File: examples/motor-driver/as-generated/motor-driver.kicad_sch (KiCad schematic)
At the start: 15 parts, among them J1 VM 2.7-10.8V, J2 MOTOR A, J3 MOTOR B, J4 LOGIC, U1 DRV8833PW

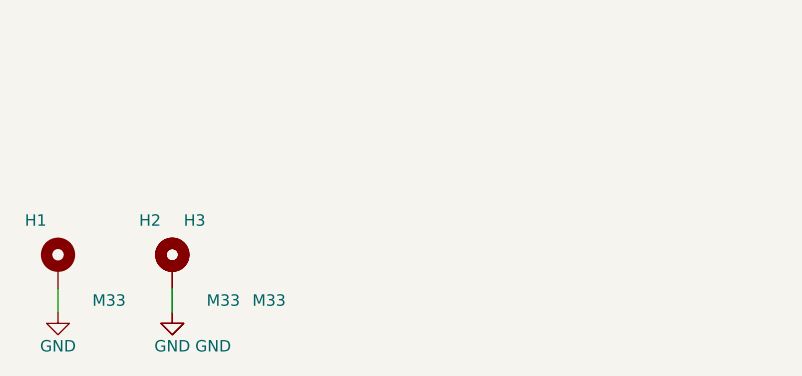
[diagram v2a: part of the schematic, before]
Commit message: Give the assembly machine something to aim at
Fiducials: three copper dots in bare mask windows, near three different
corners so a pick-and-place gets rotation as well as offset. It aligns
to the board, not to the drawing - without them it has only the routed
outline, cut to a tolerance ten times looser than the placement a 0.5 mm
pitch part is asking for. `fab.no_fiducials` reports a fine-pitch board
that has none, as context rather than as a fault: plenty of boards are
built one at a time with tweezers.

They share the corner search with the mounting holes, which is where
this found a real bug: `_courtyard_box` read lines and rectangles only,
and a mounting hole draws its courtyard as one circle - so every hole
measured as taking up no room at all, and the first three fiducials
landed on top of three screw holes. Circles and arcs count now.

Co-Authored-By: Claude Fable 5 <noreply@anthropic.com>
Claude-Session: https://claude.ai/code/session_01DUj7Ltu92tWg159mCSacwY
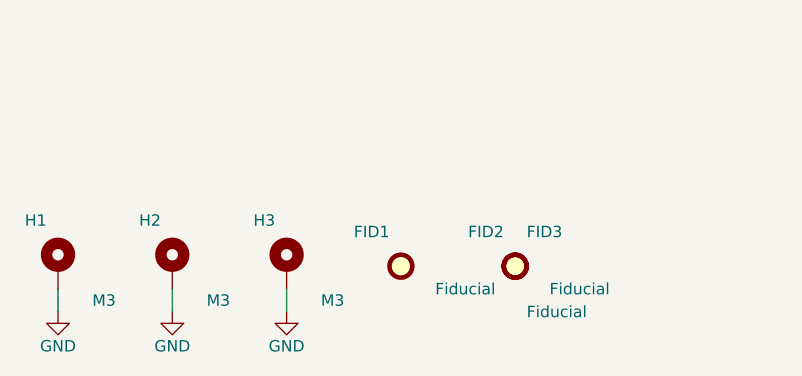
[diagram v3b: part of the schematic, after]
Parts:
- added FID1, FID2, FID3: Fiducial, Fiducial:Fiducial_1mm_Mask2mm, symbol Mechanical:Fiducial
- H1, H2, H3: value M33 -> M3
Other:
- moved on the sheet: H3
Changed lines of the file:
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@@
     (exclude_from_sim no) (in_bom yes) (on_board yes) (dnp no)
     (property "Reference" "H1" (at 24.44 164.91 0) (effects (font (size 1.27 1.27)) (justify right)))
-    (property "Value" "M33" (at 29.52 173.8 0) (effects (font (size 1.27 1.27)) (justify left)))
+    (property "Value" "M3" (at 29.52 173.8 0) (effects (font (size 1.27 1.27)) (justify left)))
     (property "Footprint" "MountingHole:MountingHole_3.2mm_M3_Pad" (at 25.71 169.99 0) (effects (font (size 1.27 1.27)) hide))
     (property "Datasheet" "~" (at 25.71 169.99 0) (effects (font (size 1.27 1.27)) hide))
@@
     (exclude_from_sim no) (in_bom yes) (on_board yes) (dnp no)
     (property "Reference" "H2" (at 37.14 164.91 0) (effects (font (size 1.27 1.27)) (justify right)))
-    (property "Value" "M33" (at 42.22 173.8 0) (effects (font (size 1.27 1.27)) (justify left)))
+    (property "Value" "M3" (at 42.22 173.8 0) (effects (font (size 1.27 1.27)) (justify left)))
     (property "Footprint" "MountingHole:MountingHole_3.2mm_M3_Pad" (at 38.41 169.99 0) (effects (font (size 1.27 1.27)) hide))
     (property "Datasheet" "~" (at 38.41 169.99 0) (effects (font (size 1.27 1.27)) hide))
@@
     (instances (project "motor-driver" (path "/bddeec65-fa67-5f6a-9af2-d98e98d56e38" (reference "H2") (unit 1))))
   )
-  (wire (pts (xy 38.41 172.53) (xy 38.41 175.07)) (stroke (width 0) (type default)))
-  (symbol (lib_id "Mechanical:MountingHole_Pad") (at 38.41 169.99 0.0) (unit 1)
+  (wire (pts (xy 51.11 172.53) (xy 51.11 175.07)) (stroke (width 0) (type default)))
+  (symbol (lib_id "Mechanical:MountingHole_Pad") (at 51.11 169.99 0.0) (unit 1)
     (exclude_from_sim no) (in_bom yes) (on_board yes) (dnp no)
-    (property "Reference" "H3" (at 39.68 164.91 0) (effects (font (size 1.27 1.27)) (justify left)))
-    (property "Value" "M33" (at 47.3 173.8 0) (effects (font (size 1.27 1.27)) (justify left)))
-    (property "Footprint" "MountingHole:MountingHole_3.2mm_M3_Pad" (at 38.41 169.99 0) (effects (font (size 1.27 1.27)) hide))
-    (property "Datasheet" "~" (at 38.41 169.99 0) (effects (font (size 1.27 1.27)) hide))
+    (property "Reference" "H3" (at 49.84 164.91 0) (effects (font (size 1.27 1.27)) (justify right)))
+    (property "Value" "M3" (at 54.92 173.8 0) (effects (font (size 1.27 1.27)) (justify left)))
+    (property "Footprint" "MountingHole:MountingHole_3.2mm_M3_Pad" (at 51.11 169.99 0) (effects (font (size 1.27 1.27)) hide))
+    (property "Datasheet" "~" (at 51.11 169.99 0) (effects (font (size 1.27 1.27)) hide))
     (pin "1" (uuid "b09ff8b6-9110-54ce-9289-a4d5206e7444-p1"))
     (instances (project "motor-driver" (path "/bddeec65-fa67-5f6a-9af2-d98e98d56e38" (reference "H3") (unit 1))))
+  )
+  (symbol (lib_id "Mechanical:Fiducial") (at 63.81 169.99 0.0) (unit 1)
+    (exclude_from_sim no) (in_bom yes) (on_board yes) (dnp no)
+    (property "Reference" "FID1" (at 62.54 166.18 0) (effects (font (size 1.27 1.27)) (justify right)))
+    (property "Value" "Fiducial" (at 67.62 172.53 0) (effects (font (size 1.27 1.27)) (justify left)))
+    (property "Footprint" "Fiducial:Fiducial_1mm_Mask2mm" (at 63.81 169.99 0) (effects (font (size 1.27 1.27)) hide))
+    (property "Datasheet" "~" (at 63.81 169.99 0) (effects (font (size 1.27 1.27)) hide))
+    (instances (project "motor-driver" (path "/bddeec65-fa67-5f6a-9af2-d98e98d56e38" (reference "FID1") (unit 1))))
+  )
+  (symbol (lib_id "Mechanical:Fiducial") (at 76.51 169.99 0.0) (unit 1)
+    (exclude_from_sim no) (in_bom yes) (on_board yes) (dnp no)
+    (property "Reference" "FID2" (at 75.24 166.18 0) (effects (font (size 1.27 1.27)) (justify right)))
+    (property "Value" "Fiducial" (at 80.32 172.53 0) (effects (font (size 1.27 1.27)) (justify left)))
+    (property "Footprint" "Fiducial:Fiducial_1mm_Mask2mm" (at 76.51 169.99 0) (effects (font (size 1.27 1.27)) hide))
+    (property "Datasheet" "~" (at 76.51 169.99 0) (effects (font (size 1.27 1.27)) hide))
+    (instances (project "motor-driver" (path "/bddeec65-fa67-5f6a-9af2-d98e98d56e38" (reference "FID2") (unit 1))))
+  )
+  (symbol (lib_id "Mechanical:Fiducial") (at 76.51 169.99 0.0) (unit 1)
+    (exclude_from_sim no) (in_bom yes) (on_board yes) (dnp no)
+    (property "Reference" "FID3" (at 77.78 166.18 0) (effects (font (size 1.27 1.27)) (justify left)))
+    (property "Value" "Fiducial" (at 77.78 175.07 0) (effects (font (size 1.27 1.27)) (justify left)))
+    (property "Footprint" "Fiducial:Fiducial_1mm_Mask2mm" (at 76.51 169.99 0) (effects (font (size 1.27 1.27)) hide))
+    (property "Datasheet" "~" (at 76.51 169.99 0) (effects (font (size 1.27 1.27)) hide))
+    (instances (project "motor-driver" (path "/bddeec65-fa67-5f6a-9af2-d98e98d56e38" (reference "FID3") (unit 1))))
   )
   (wire (pts (xy 46.03 82.36) (xy 53.65 82.36)) (stroke (width 0) (type default)))
@@
     (instances (project "motor-driver" (path "/bddeec65-fa67-5f6a-9af2-d98e98d56e38" (reference "#PWR10") (unit 1))))
   )
-  (symbol (lib_id "power:GND") (at 38.41 175.07 0) (unit 1)
+  (symbol (lib_id "power:GND") (at 51.11 175.07 0) (unit 1)
     (exclude_from_sim no) (in_bom no) (on_board yes) (dnp no)
-    (property "Reference" "#PWR11" (at 38.41 175.07 0) (effects (font (size 1.27 1.27)) hide))
-    (property "Value" "GND" (at 40.95 178.88 0) (effects (font (size 1.27 1.27)) (justify left)))
-    (property "Footprint" "" (at 38.41 175.07 0) (effects (font (size 1.27 1.27)) hide))
-    (property "Datasheet" "" (at 38.41 175.07 0) (effects (font (size 1.27 1.27)) hide))
+    (property "Reference" "#PWR11" (at 51.11 175.07 0) (effects (font (size 1.27 1.27)) hide))
+    (property "Value" "GND" (at 51.11 178.88 0) (effects (font (size 1.27 1.27))))
+    (property "Footprint" "" (at 51.11 175.07 0) (effects (font (size 1.27 1.27)) hide))
+    (property "Datasheet" "" (at 51.11 175.07 0) (effects (font (size 1.27 1.27)) hide))
     (pin "1" (uuid "36f47f82-b430-5f2e-8c28-879d8277211b-p"))
     (instances (project "motor-driver" (path "/bddeec65-fa67-5f6a-9af2-d98e98d56e38" (reference "#PWR11") (unit 1))))

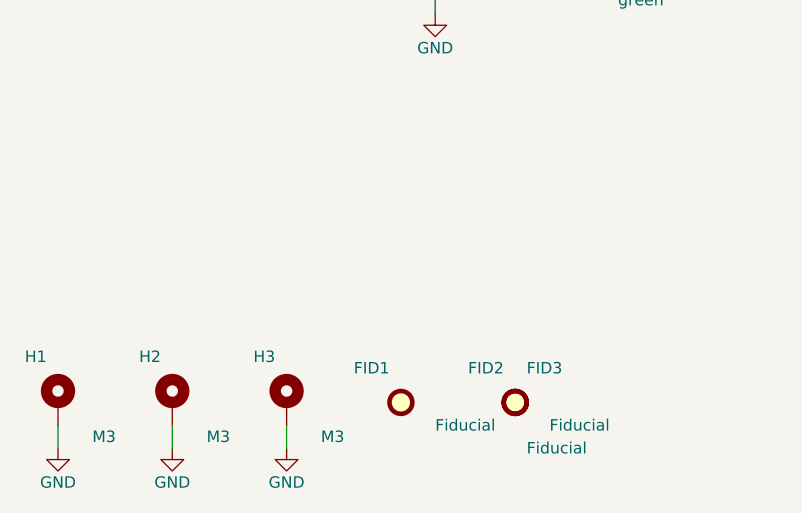
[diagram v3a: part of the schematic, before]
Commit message: Let the new parts sit somewhere sensible, on the board and on the sheet
Placing screw holes and fiducials turned up four things that were wrong
before either existed, all of them about where something is allowed to
go rather than about the parts themselves.

A designator was kept off the pads but not inside the board outline, so
any part at the edge - a connector, and now a hole - had its reference
clipped by the edge. Every board had been carrying one or two of those.

A symbol with no pins leaves no trace in the sheet planner's obstacle
list, because that list is built from pin stubs. The screw holes were
invisible to it and the fiducials landed on top of them. The free-row
search also ran off the right-hand edge of an A4 page and sat over the
title block on the way, which is `readability.outside_page` and
`readability.margin_intrusion` respectively - both real, both now
avoided by bounding the search to the drawing area.

And the bill-of-materials flag is read from the footprint rather than
the symbol library, because the footprint is the side KiCad's parity
check reads and the side the fab agrees with. That retired three
warnings the op-amp board had been carrying since it gained test
points: `Connector:TestPoint` claims to be a BOM line and its own
footprint says otherwise.

All four fast boards pass their gates; the suite is green on 10.0.4.

Co-Authored-By: Claude Fable 5 <noreply@anthropic.com>
Claude-Session: https://claude.ai/code/session_01DUj7Ltu92tWg159mCSacwY
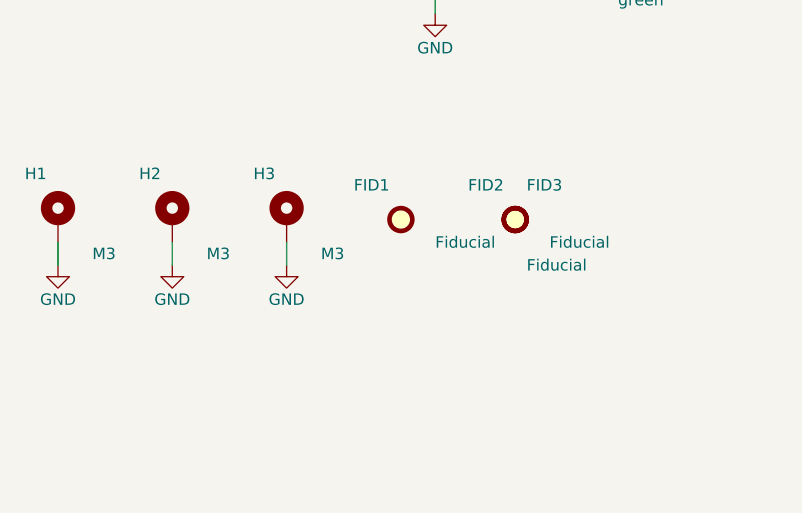
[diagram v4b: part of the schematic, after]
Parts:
- FID1, FID2, FID3, H1, H2, H3: now left out of the parts list
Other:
- moved on the sheet: FID1, FID2, FID3, H1, H2, H3

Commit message: Put the vias back where the copper moved, and let the fillets vote
The FPGA board came back from its re-route with two unconnected nets and
three dangling ends, and the cause was older than anything this round
added. The router hands back a via for every layer change; six passes
then reshape the copper - snapping to 45s, chamfering, spreading folds,
and now filleting - and none of them move the holes underneath. A joint
that slides a millimetre from its via is two loose ends and one broken
net, and `_unlooped` then swept the via away as orphaned, because it
kept a via only when a track ended on its exact coordinate.

Two fixes, both about what "connected" means. A via lives if kept copper
*touches* it, not if a coordinate matches. And a new `_joined` pass
re-derives the joints from the copper that actually got written: where a
net ends on two layers at one point with no via reaching it, one goes
back in. It reads the finished geometry, so it cannot drift the way six
separate passes carrying vias along with them would.

The same reasoning fixes two rules that had been measuring coordinates
rather than copper. `route.stub` matched a track end to a via's centre
exactly, and called a joint a stub whenever a reshaping pass had moved
it a quarter of a millimetre inside the very barrel it was connected to.
`route.width_step` walked a neck back to its pad and stopped at the
first width change - which, on a filleted board, is the teardrop, so
every escape's neck stopped being recognised as one.

While the three copies of the post-route pipeline were being edited for
the third time this session, they became one function. That is how
`_teardrops` had come to run on two of the three exits.

All five boards: DRC clean on both matrix versions, nothing unconnected.
Four pass their gates; the FPGA board is down to the two-layer bill it
has always had - four nets over plane cuts and one 88 degree corner.

Co-Authored-By: Claude Fable 5 <noreply@anthropic.com>
Claude-Session: https:/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
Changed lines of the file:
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@@
     (exclude_from_sim no) (in_bom no) (on_board yes) (dnp no)
     (property "Reference" "H1" (at 24.44 144.59 0) (effects (font (size 1.27 1.27)) (justify right)))
-    (property "Value" "M3" (at 29.52 153.48 0) (effects (font (size 1.27 1.27)) (justify left)))
+    (property "Value" "M3" (at 29.52 153.48 0) (effects (font (size 1.27 1.27)) (justify left) hide))
     (property "Footprint" "MountingHole:MountingHole_3.2mm_M3_Pad" (at 25.71 149.67 0) (effects (font (size 1.27 1.27)) hide))
     (property "Datasheet" "~" (at 25.71 149.67 0) (effects (font (size 1.27 1.27)) hide))
@@
     (exclude_from_sim no) (in_bom no) (on_board yes) (dnp no)
     (property "Reference" "H2" (at 37.14 144.59 0) (effects (font (size 1.27 1.27)) (justify right)))
-    (property "Value" "M3" (at 42.22 153.48 0) (effects (font (size 1.27 1.27)) (justify left)))
+    (property "Value" "M3" (at 42.22 153.48 0) (effects (font (size 1.27 1.27)) (justify left) hide))
     (property "Footprint" "MountingHole:MountingHole_3.2mm_M3_Pad" (at 38.41 149.67 0) (effects (font (size 1.27 1.27)) hide))
     (property "Datasheet" "~" (at 38.41 149.67 0) (effects (font (size 1.27 1.27)) hide))
@@
     (exclude_from_sim no) (in_bom no) (on_board yes) (dnp no)
     (property "Reference" "H3" (at 49.84 144.59 0) (effects (font (size 1.27 1.27)) (justify right)))
-    (property "Value" "M3" (at 54.92 153.48 0) (effects (font (size 1.27 1.27)) (justify left)))
+    (property "Value" "M3" (at 54.92 153.48 0) (effects (font (size 1.27 1.27)) (justify left) hide))
     (property "Footprint" "MountingHole:MountingHole_3.2mm_M3_Pad" (at 51.11 149.67 0) (effects (font (size 1.27 1.27)) hide))
     (property "Datasheet" "~" (at 51.11 149.67 0) (effects (font (size 1.27 1.27)) hide))
@@
     (exclude_from_sim no) (in_bom no) (on_board yes) (dnp no)
     (property "Reference" "FID1" (at 62.54 145.86 0) (effects (font (size 1.27 1.27)) (justify right)))
-    (property "Value" "Fiducial" (at 67.62 152.21 0) (effects (font (size 1.27 1.27)) (justify left)))
+    (property "Value" "Fiducial" (at 67.62 152.21 0) (effects (font (size 1.27 1.27)) (justify left) hide))
     (property "Footprint" "Fiducial:Fiducial_1mm_Mask2mm" (at 63.81 149.67 0) (effects (font (size 1.27 1.27)) hide))
     (property "Datasheet" "~" (at 63.81 149.67 0) (effects (font (size 1.27 1.27)) hide))
@@
     (exclude_from_sim no) (in_bom no) (on_board yes) (dnp no)
     (property "Reference" "FID2" (at 75.24 145.86 0) (effects (font (size 1.27 1.27)) (justify right)))
-    (property "Value" "Fiducial" (at 80.32 152.21 0) (effects (font (size 1.27 1.27)) (justify left)))
+    (property "Value" "Fiducial" (at 80.32 152.21 0) (effects (font (size 1.27 1.27)) (justify left) hide))
     (property "Footprint" "Fiducial:Fiducial_1mm_Mask2mm" (at 76.51 149.67 0) (effects (font (size 1.27 1.27)) hide))
     (property "Datasheet" "~" (at 76.51 149.67 0) (effects (font (size 1.27 1.27)) hide))
@@
     (exclude_from_sim no) (in_bom no) (on_board yes) (dnp no)
     (property "Reference" "FID3" (at 77.78 145.86 0) (effects (font (size 1.27 1.27)) (justify left)))
-    (property "Value" "Fiducial" (at 77.78 154.75 0) (effects (font (size 1.27 1.27)) (justify left)))
+    (property "Value" "Fiducial" (at 77.78 154.75 0) (effects (font (size 1.27 1.27)) (justify left) hide))
     (property "Footprint" "Fiducial:Fiducial_1mm_Mask2mm" (at 76.51 149.67 0) (effects (font (size 1.27 1.27)) hide))
     (property "Datasheet" "~" (at 76.51 149.67 0) (effects (font (size 1.27 1.27)) hide))

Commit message: Leave room for the screw, and print the ink where the board is
The screw holes were placed against the hole's own courtyard, which is the
drill plus a whisker - so on four of the five boards a hole sat inside a
connector's mating space, closest 0.42 mm. What goes through an M3 hole is a
pan head on a washer, seven millimetres of steel lying flat, and a connector
wants its shell, its wires and the fingers that fit them on top of that. The
spot search now keeps the fastener's own circle clear of every part body and
gives connectors CONNECTOR_ACCESS more, and three rules say so when a board
does not: mechanical.fastener_clearance, mechanical.connector_access and
mechanical.fastener_copper, all blocking for a generated design.

Silk was measured with a per-character advance of 0.78, and KiCad's stroke
font is proportional at 0.94 to 1.07. Everything downstream of that estimate
was placing ink where it did not fit: a legend across a capacitor's land, a
designator through the board's own name. `_text_extent` takes the top of the
measured range, adds the fab's clearance and is used by every silk placement.

Three placements also fell through to a position nobody chose. A designator
that found nothing kept its library offset, which for a part in a corner
points off the board; the board id took the first of eight fixed strips; a
legend took the least bad of six spots. All three are scored now, over
candidate sets wide enough to have an answer - and a pad-less footprint, which
is what a mounting hole is, is no longer skipped outright.

silk.off_board reports the case KiCad's own test cannot: ink that clears the
edge entirely is never printed, and DRC only measures ink that crosses it.

_unspiked redraws a corner tighter than a right angle as the elbow between its
neighbours - one diagonal, one straight, no step back to a heading the line
has already left. It is never longer than what it replaces.

All four fast boards: 0 errors, 0 warnings.

Co-Authored-By: Claude Fable 5 <no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
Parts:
- removed FID3: Fiducial, Fiducial:Fiducial_1mm_Mask2mm, symbol Mechanical:Fiducial
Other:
- moved on the sheet: FID2
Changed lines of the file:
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@@
     (instances (project "motor-driver" (path "/bddeec65-fa67-5f6a-9af2-d98e98d56e38" (reference "FID1") (unit 1))))
   )
-  (symbol (lib_id "Mechanical:Fiducial") (at 76.51 149.67 0.0) (unit 1)
+  (symbol (lib_id "Mechanical:Fiducial") (at 63.81 149.67 0.0) (unit 1)
     (exclude_from_sim no) (in_bom no) (on_board yes) (dnp no)
-    (property "Reference" "FID2" (at 75.24 145.86 0) (effects (font (size 1.27 1.27)) (justify right)))
-    (property "Value" "Fiducial" (at 80.32 152.21 0) (effects (font (size 1.27 1.27)) (justify left) hide))
-    (property "Footprint" "Fiducial:Fiducial_1mm_Mask2mm" (at 76.51 149.67 0) (effects (font (size 1.27 1.27)) hide))
-    (property "Datasheet" "~" (at 76.51 149.67 0) (effects (font (size 1.27 1.27)) hide))
+    (property "Reference" "FID2" (at 65.08 145.86 0) (effects (font (size 1.27 1.27)) (justify left)))
+    (property "Value" "Fiducial" (at 65.08 154.75 0) (effects (font (size 1.27 1.27)) (justify left) hide))
+    (property "Footprint" "Fiducial:Fiducial_1mm_Mask2mm" (at 63.81 149.67 0) (effects (font (size 1.27 1.27)) hide))
+    (property "Datasheet" "~" (at 63.81 149.67 0) (effects (font (size 1.27 1.27)) hide))
     (instances (project "motor-driver" (path "/bddeec65-fa67-5f6a-9af2-d98e98d56e38" (reference "FID2") (unit 1))))
   )
-  (symbol (lib_id "Mechanical:Fiducial") (at 76.51 149.67 0.0) (unit 1)
-    (exclude_from_sim no) (in_bom no) (on_board yes) (dnp no)
-    (property "Reference" "FID3" (at 77.78 145.86 0) (effects (font (size 1.27 1.27)) (justify left)))
-    (property "Value" "Fiducial" (at 77.78 154.75 0) (effects (font (size 1.27 1.27)) (justify left) hide))
-    (property "Footprint" "Fiducial:Fiducial_1mm_Mask2mm" (at 76.51 149.67 0) (effects (font (size 1.27 1.27)) hide))
-    (property "Datasheet" "~" (at 76.51 149.67 0) (effects (font (size 1.27 1.27)) hide))
-    (instances (project "motor-driver" (path "/bddeec65-fa67-5f6a-9af2-d98e98d56e38" (reference "FID3") (unit 1))))
-  )
   (wire (pts (xy 46.03 82.36) (xy 53.65 82.36)) (stroke (width 0) (type default)))
